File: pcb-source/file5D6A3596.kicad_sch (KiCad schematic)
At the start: 23 parts, among them J2 Program_enable, J4 UPDI, J6 Conn_02x03_Odd_Even, U2 MAX3232, U5 MCP795xx, Y1 32KHz

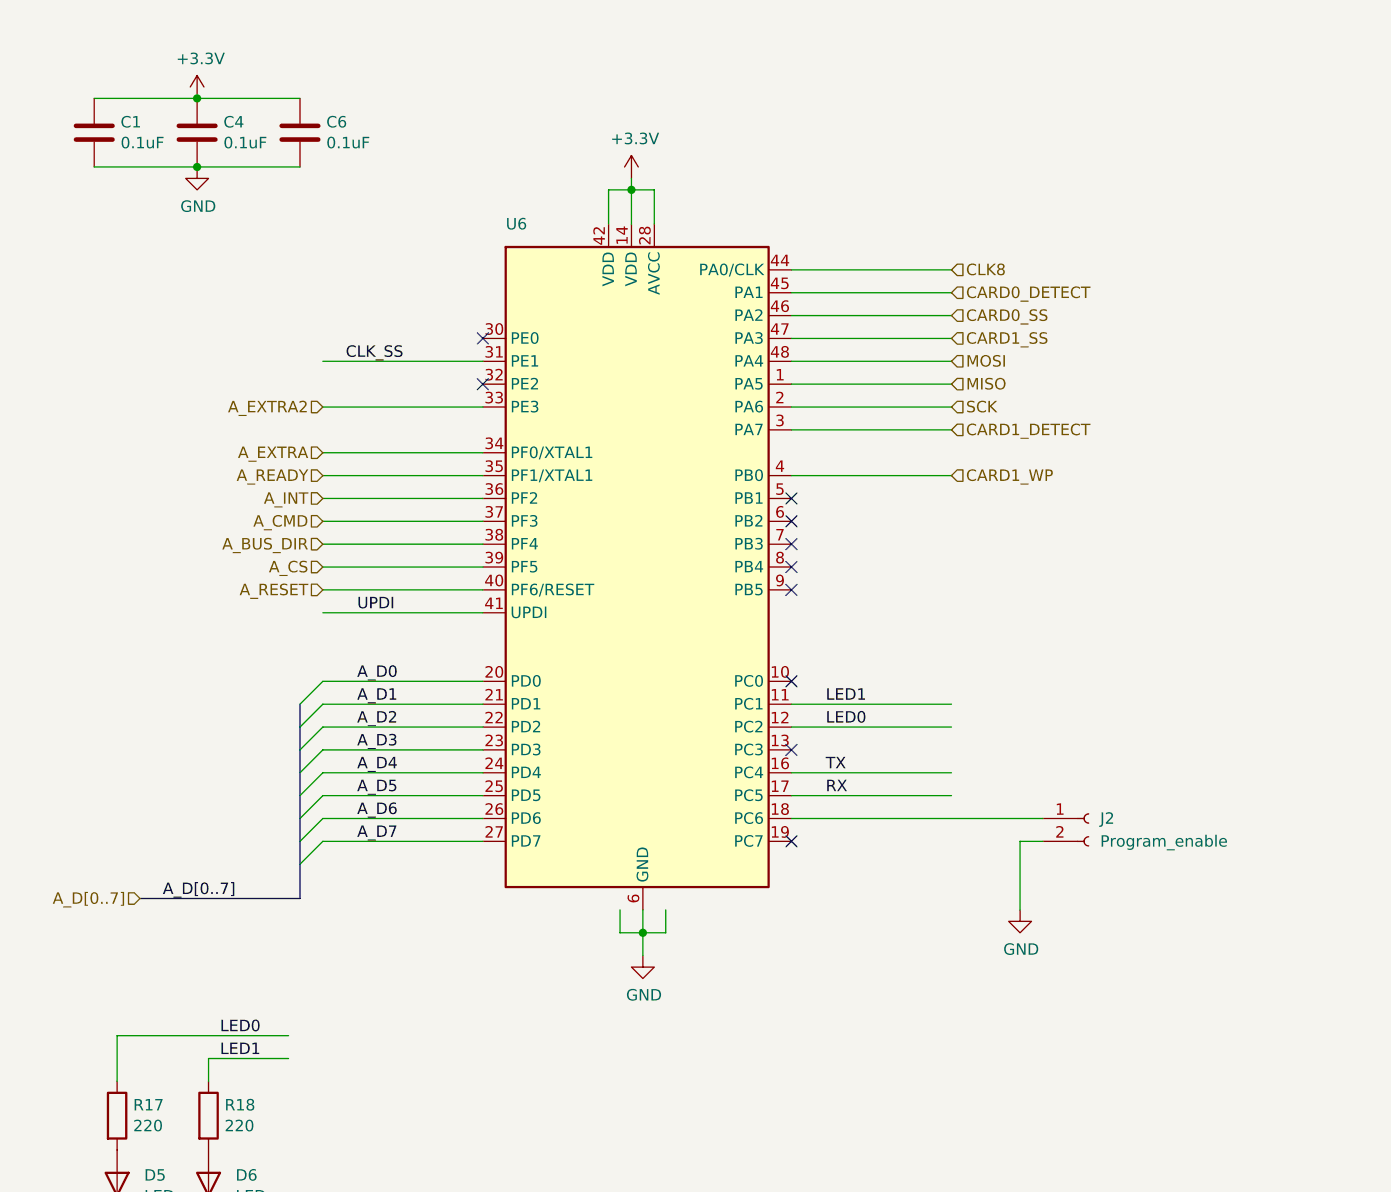
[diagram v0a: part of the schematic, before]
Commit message: Switched the avr128da to an stm32c031
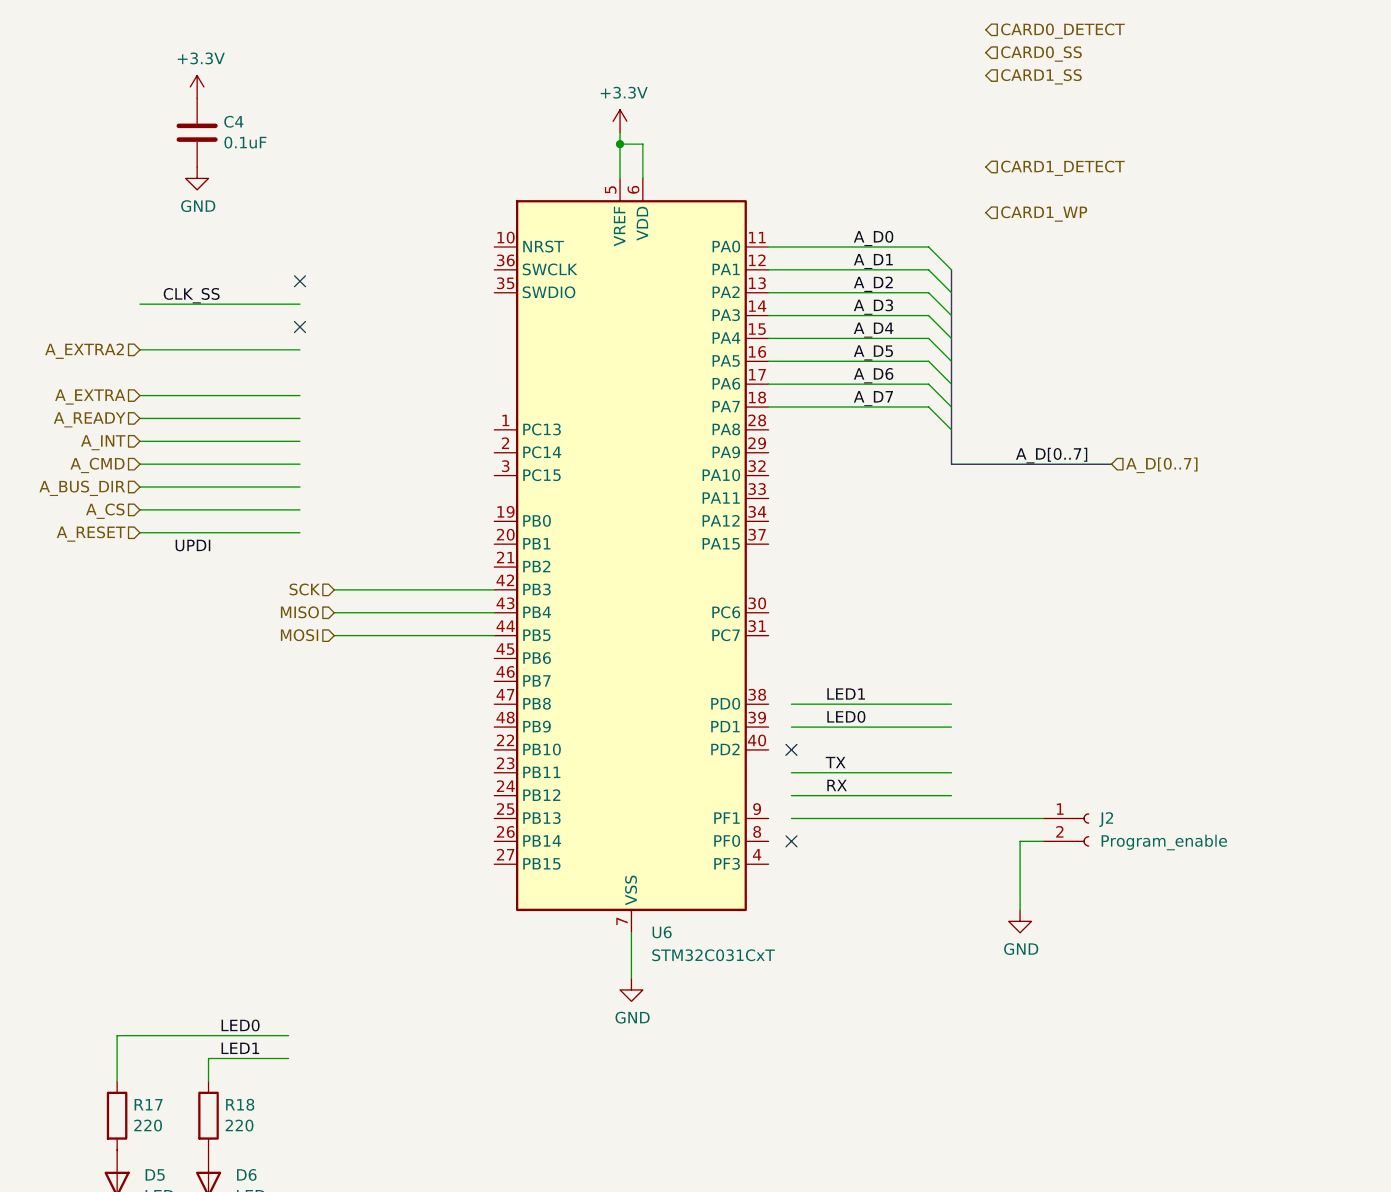
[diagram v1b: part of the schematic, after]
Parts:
- removed C1, C6: 0.1uF, Capacitor_SMD:C_0603_1608Metric, symbol Device:C
- removed U6: ~, Package_QFP:LQFP-48_7x7mm_P0.5mm, symbol Simon:AVR128DA-48
- added U6: STM32C031CxT, Package_QFP:LQFP-48_7x7mm_P0.5mm, symbol Simon:STM32C031CxT
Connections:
- net +3V3: now also U6.5 (VREF), U6.6 (VDD)
- net A_D0: now also U6.11 (PA0)
- net A_D1: now also U6.12 (PA1)
- net A_D2: now also U6.13 (PA2)
- net A_D3: now also U6.14 (PA3)
- net A_D4: now also U6.15 (PA4)
- net A_D5: now also U6.16 (PA5)
- net A_D6: now also U6.17 (PA6)
- net A_D7: now also U6.18 (PA7)
- net GND: now also U6.7 (VSS)
- net MISO: now also U6.43 (PB4)
- net MOSI: now also U6.44 (PB5)
- net SCK: now also U6.42 (PB3)
- no-connect marks 16 -> 10

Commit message: Final board setup that was sent to production
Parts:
- removed J4: UPDI, Connector_PinHeader_2.54mm:PinHeader_2x03_P2.54mm_Vertical, symbol Connector_Generic:Conn_02x03_Odd_Even
- added J7: ST-LINK, Connector_PinHeader_2.54mm:PinHeader_2x05_P2.54mm_Vertical, symbol Connector_Generic:Conn_02x05_Odd_Even
- Y1: footprint Crystal:Crystal_C38-LF_D3.0mm_L8.0mm_Vertical -> simon:Crystal_SMD_ECX_31B-2Pin_3.2x1.5mm
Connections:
- net A_BUS_DIR: now also U6.20 (PB1)
- net A_CMD: now also U6.21 (PB2)
- net A_CS: now also U6.19 (PB0)
- net A_EXTRA: now also U6.23 (PB11)
- net A_EXTRA2: now also U6.22 (PB10)
- net A_INT: now also U6.9 (PF1)
- net A_READY: now also U6.8 (PF0)
- net A_RESET: now also U6.10 (NRST), J7.1 (Pin_1)
- net CARD0_DETECT: now also U6.30 (PC6)
- net CARD0_SS: now also U6.31 (PC7)
- net CARD1_DETECT: now also U6.33 (PA11)
- net CARD1_SS: now also U6.32 (PA10)
- net CARD1_WP: now also U6.34 (PA12)
- net CLK_SS: now also U6.40 (PD2)
- net GND: now also J7.5 (Pin_5), J7.6 (Pin_6)
- net LED0: now also U6.2 (PC14)
- net LED1: now also U6.1 (PC13)
- net RX: now also U6.46 (PB7)
- net TX: now also U6.45 (PB6)
- net CLKOUT: now reaches U6.28 (PA8)
- net at U6.29 (PA9): now also J2.1 (Pin_1)
- net SWDIO: now reaches U6.35 (SWDIO)
- net SWDIO: now also J7.4 (Pin_4)
- net SWCLK: now reaches U6.36 (SWCLK)
- net SWCLK: now also J7.2 (Pin_2)
- no-connect marks 10 -> 19
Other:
- moved on the sheet: C10, C2, C21, C22, C7, J2, J6, U2

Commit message: New changes as I slowly port the code to the new board
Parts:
- R17: value 220 -> 470
- R18: value 220 -> 2K
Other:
- note added: "GREEN"
- note added: "RED"
- moved on the sheet: D5, D6, R17, R18
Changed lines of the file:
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@@
   (junction (at 100.33 176.53) (diameter 0) (color 0 0 0 0)
   )
-  (junction (at 29.21 149.86) (diameter 0) (color 0 0 0 0)
+  (junction (at 38.1 148.59) (diameter 0) (color 0 0 0 0)
   )
   (junction (at 252.73 91.44) (diameter 0) (color 0 0 0 0)
@@
     (stroke (width 0) (type default))
   )
-  (wire (pts (xy 24.13 147.32) (xy 24.13 149.86))
-    (stroke (width 0) (type default))
-  )
-  (wire (pts (xy 29.21 149.86) (xy 34.29 149.86))
+  (wire (pts (xy 33.02 146.05) (xy 33.02 148.59))
+    (stroke (width 0) (type default))
+  )
+  (wire (pts (xy 38.1 148.59) (xy 43.18 148.59))
     (stroke (width 0) (type default))
   )
@@
     (stroke (width 0) (type default))
   )
-  (wire (pts (xy 34.29 147.32) (xy 34.29 149.86))
+  (wire (pts (xy 43.18 146.05) (xy 43.18 148.59))
     (stroke (width 0) (type default))
   )
@@
     (stroke (width 0) (type default))
   )
-  (wire (pts (xy 24.13 132.08) (xy 24.13 127))
+  (wire (pts (xy 33.02 130.81) (xy 33.02 125.73))
     (stroke (width 0) (type default))
   )
@@
     (stroke (width 0) (type default))
   )
-  (wire (pts (xy 34.29 132.08) (xy 34.29 129.54))
+  (wire (pts (xy 43.18 130.81) (xy 43.18 128.27))
     (stroke (width 0) (type default))
   )
@@
     (stroke (width 0) (type default))
   )
-  (wire (pts (xy 34.29 129.54) (xy 43.18 129.54))
+  (wire (pts (xy 43.18 128.27) (xy 52.07 128.27))
     (stroke (width 0) (type default))
   )
@@
     (stroke (width 0) (type default))
   )
-  (wire (pts (xy 24.13 149.86) (xy 29.21 149.86))
+  (wire (pts (xy 33.02 148.59) (xy 38.1 148.59))
     (stroke (width 0) (type default))
   )
@@
     (stroke (width 0) (type default))
   )
-  (wire (pts (xy 24.13 127) (xy 43.18 127))
+  (wire (pts (xy 33.02 125.73) (xy 52.07 125.73))
     (stroke (width 0) (type default))
   )
   (wire (pts (xy 187.96 106.68) (xy 196.85 106.68))
     (stroke (width 0) (type default))
+  )
+  (text "GREEN" (at 52.07 135.89 0)
+    (effects (font (size 1.27 1.27)) (justify left bottom))
+  )
+  (text "RED" (at 24.13 135.89 0)
+    (effects (font (size 1.27 1.27)) (justify left bottom))
   )
   (label "A_D2" (at 110.49 44.45 180) (fields_autoplaced)
@@
     (effects (font (size 1.27 1.27)) (justify left bottom))
   )
-  (label "LED0" (at 35.56 127 0) (fields_autoplaced)
+  (label "LED0" (at 44.45 125.73 0) (fields_autoplaced)
     (effects (font (size 1.27 1.27)) (justify left bottom))
   )
@@
     (effects (font (size 1.27 1.27)) (justify right bottom))
   )
-  (label "LED1" (at 35.56 129.54 0) (fields_autoplaced)
+  (label "LED1" (at 44.45 128.27 0) (fields_autoplaced)
     (effects (font (size 1.27 1.27)) (justify left bottom))
   )
@@
     )
   )
-  (symbol (lib_id "Device:R") (at 34.29 135.89 0) (unit 1)
-    (in_bom yes) (on_board yes) (dnp no)
-    (property "Reference" "R18" (at 36.068 134.7216 0)
-      (effects (font (size 1.27 1.27)) (justify left))
-    )
-    (property "Value" "220" (at 36.068 137.033 0)
-      (effects (font (size 1.27 1.27)) (justify left))
-    )
-    (property "Footprint" "Resistor_SMD:R_0805_2012Metric" (at 32.512 135.89 90)
-      (effects (font (size 1.27 1.27)) hide)
-    )
-    (property "Datasheet" "~" (at 34.29 135.89 0)
+  (symbol (lib_id "Device:R") (at 43.18 134.62 0) (unit 1)
+    (in_bom yes) (on_board yes) (dnp no)
+    (property "Reference" "R18" (at 44.958 133.4516 0)
+      (effects (font (size 1.27 1.27)) (justify left))
+    )
+    (property "Value" "2K" (at 44.958 135.763 0)
+      (effects (font (size 1.27 1.27)) (justify left))
+    )
+    (property "Footprint" "Resistor_SMD:R_0805_2012Metric" (at 41.402 134.62 90)
+      (effects (font (size 1.27 1.27)) hide)
+    )
+    (property "Datasheet" "~" (at 43.18 134.62 0)
       (effects (font (size 1.27 1.27)) hide)
     )
@@
     )
   )
-  (symbol (lib_id "Device:LED") (at 34.29 143.51 90) (unit 1)
-    (in_bom yes) (on_board yes) (dnp no)
-    (property "Reference" "D6" (at 37.2872 142.5194 90)
+  (symbol (lib_id "Device:LED") (at 43.18 142.24 90) (unit 1)
+    (in_bom yes) (on_board yes) (dnp no)
+    (property "Reference" "D6" (at 46.1772 141.2494 90)
       (effects (font (size 1.27 1.27)) (justify right))
     )
-    (property "Value" "LED" (at 37.2872 144.8308 90)
+    (property "Value" "LED" (at 46.1772 143.5608 90)
       (effects (font (size 1.27 1.27)) (justify right))
     )
-    (property "Footprint" "LED_THT:LED_D3.0mm_Horizontal_O1.27mm_Z2.0mm" (at 34.29 143.51 0)
-      (effects (font (size 1.27 1.27)) hide)
-    )
-    (property "Datasheet" "~" (at 34.29 143.51 0)
+    (property "Footprint" "LED_THT:LED_D3.0mm_Horizontal_O1.27mm_Z2.0mm" (at 43.18 142.24 0)
+      (effects (font (size 1.27 1.27)) hide)
+    )
+    (property "Datasheet" "~" (at 43.18 142.24 0)
       (effects (font (size 1.27 1.27)) hide)
     )
@@
     )
   )
-  (symbol (lib_id "power:GND") (at 29.21 149.86 0) (unit 1)
-    (in_bom yes) (on_board yes) (dnp no)
-    (property "Reference" "#PWR023" (at 29.21 156.21 0)
-      (effects (font (size 1.27 1.27)) hide)
-    )
-    (property "Value" "GND" (at 29.337 154.2542 0)
-      (effects (font (size 1.27 1.27)))
-    )
-    (property "Footprint" "" (at 29.21 149.86 0)
-      (effects (font (size 1.27 1.27)) hide)
-    )
-    (property "Datasheet" "" (at 29.21 149.86 0)
+  (symbol (lib_id "power:GND") (at 38.1 148.59 0) (unit 1)
+    (in_bom yes) (on_board yes) (dnp no)
+    (property "Reference" "#PWR023" (at 38.1 154.94 0)
+      (effects (font (size 1.27 1.27)) hide)
+    )
+    (property "Value" "GND" (at 38.227 152.9842 0)
+      (effects (font (size 1.27 1.27)))
+    )
+    (property "Footprint" "" (at 38.1 148.59 0)
+      (effects (font (size 1.27 1.27)) hide)
+    )
+    (property "Datasheet" "" (at 38.1 148.59 0)
       (effects (font (size 1.27 1.27)) hide)
     )
@@
     )
   )
-  (symbol (lib_id "Device:LED") (at 24.13 143.51 90) (unit 1)
-    (in_bom yes) (on_board yes) (dnp no)
-    (property "Reference" "D5" (at 27.1272 142.5194 90)
+  (symbol (lib_id "Device:LED") (at 33.02 142.24 90) (unit 1)
+    (in_bom yes) (on_board yes) (dnp no)
+    (property "Reference" "D5" (at 36.0172 141.2494 90)
       (effects (font (size 1.27 1.27)) (justify right))
     )
-    (property "Value" "LED" (at 27.1272 144.8308 90)
+    (property "Value" "LED" (at 36.0172 143.5608 90)
       (effects (font (size 1.27 1.27)) (justify right))
     )
-    (property "Footprint" "LED_THT:LED_D3.0mm_Horizontal_O1.27mm_Z2.0mm" (at 24.13 143.51 0)
-      (effects (font (size 1.27 1.27)) hide)
-    )
-    (property "Datasheet" "~" (at 24.13 143.51 0)
+    (property "Footprint" "LED_THT:LED_D3.0mm_Horizontal_O1.27mm_Z2.0mm" (at 33.02 142.24 0)
+      (effects (font (size 1.27 1.27)) hide)
+    )
+    (property "Datasheet" "~" (at 33.02 142.24 0)
       (effects (font (size 1.27 1.27)) hide)
     )
@@
     )
   )
-  (symbol (lib_id "Device:R") (at 24.13 135.89 0) (unit 1)
-    (in_bom yes) (on_board yes) (dnp no)
-    (property "Reference" "R17" (at 25.908 134.7216 0)
-      (effects (font (size 1.27 1.27)) (justify left))
-    )
-    (property "Value" "220" (at 25.908 137.033 0)
-      (effects (font (size 1.27 1.27)) (justify left))
-    )
-    (property "Footprint" "Resistor_SMD:R_0805_2012Metric" (at 22.352 135.89 90)
-      (effects (font (size 1.27 1.27)) hide)
-    )
-    (property "Datasheet" "~" (at 24.13 135.89 0)
-      (effects (font (size 1.27 1.27)) hide)
-    )
+  (symbol (lib_id "Device:R") (at 33.02 134.62 0) (unit 1)
+    (in_bom yes) (on_board yes) (dnp no)
+    (property "Reference" "R17" (at 34.798 133.4516 0)
+      (effects (font (size 1.27 1.27)) (justify left))
+    )
+    (property "Value" "470" (at 34.798 135.763 0)
+      (effects (font (size 1.27 1.27)) (justify left))
+    )
+    (property "Footprint" "Resistor_SMD:R_0805_2012Metric" (at 31.242 134.62 90)
+      (effects (font (size 1.27 1.27)) hide)
+    )
+    (property "Datasheet" "~" (at 33.02 134.62 0)
+      (effects (font (size 1.27 1.27)) hide)
+    )
